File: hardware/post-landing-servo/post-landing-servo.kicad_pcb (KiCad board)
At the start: 2 copper layers, 0 parts

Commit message: Gavin and Remco pcb to be checked
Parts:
- added G***: LOGO, LOGO, F.Cu at (42.9, 54.5)
- added G***: LOGO, LOGO, F.Cu at (100.3, 58.1)
- added G***: LOGO, LOGO, F.Cu at (98.7, 38.8)
- added G***: LOGO, LOGO, F.Cu at (100.0, 47.8)
- added H1: MountingHole_Pad, MountingHole:MountingHole_3.2mm_M3_Pad_Via, F.Cu at (57.2, 36.1)
- added H2: MountingHole_Pad, MountingHole:MountingHole_3.2mm_M3_Pad_Via, F.Cu at (83.2, 59.1)
- added J1: Conn_01x08, Custom:ZH-6PWB_knockoff, F.Cu at (60.0, 58.2)
- added J2: DE9_Pins, Connector_Dsub:DSUB-9_Pins_Horizontal_P2.77x2.84mm_EdgePinOffset4.94mm_Housed_MountingHolesOffset4.94mm, F.Cu at (50.6, 41.8)
- added J3: DE9_Pins, Connector_Dsub:DSUB-9_Pins_Horizontal_P2.77x2.84mm_EdgePinOffset4.94mm_Housed_MountingHolesOffset4.94mm, F.Cu at (89.5, 52.8)
- added J4: Conn_01x08, Custom:ZH-6PWB_knockoff, F.Cu at (73.2, 58.3)
- added J5: Conn_01x06, Connector_JST:JST_EH_B6B-EH-A_1x06_P2.50mm_Vertical, F.Cu at (64.8, 34.6)
- added JP1: SolderJumper_2_Open, Jumper:SolderJumper-2_P1.3mm_Bridged_Pad1.0x1.5mm, F.Cu at (63.5, 41.8)
- added JP2: SolderJumper_2_Open, Jumper:SolderJumper-2_P1.3mm_Bridged_Pad1.0x1.5mm, F.Cu at (63.6, 45.6)
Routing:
- net +5V: track 0.00 -> 126.1 mm
- net /CAN_A+: track 0.00 -> 109.2 mm
- net /CAN_A-: track 0.00 -> 108.7 mm
- net +24V: track 0.00 -> 98.6 mm
- net /SIG2: track 0.00 -> 72.3 mm, vias 0 -> 1
- net /SIG1: track 0.00 -> 68.7 mm, vias 0 -> 1
- net /CAN_B+: track 0.00 -> 64.8 mm
- net /CAN_B-: track 0.00 -> 64.7 mm
- net GND: track 0.00 -> 40.2 mm
- added copper zone on B.Cu, net GND
- added copper zone on F.Cu, net GND
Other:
- board outline added: 70.3 x 32.8 mm
- board text added: "67 67 67 67 67 67 67 67 67 67 67"
- board text added: "Designed by: Gavin, H. & Remco, S."

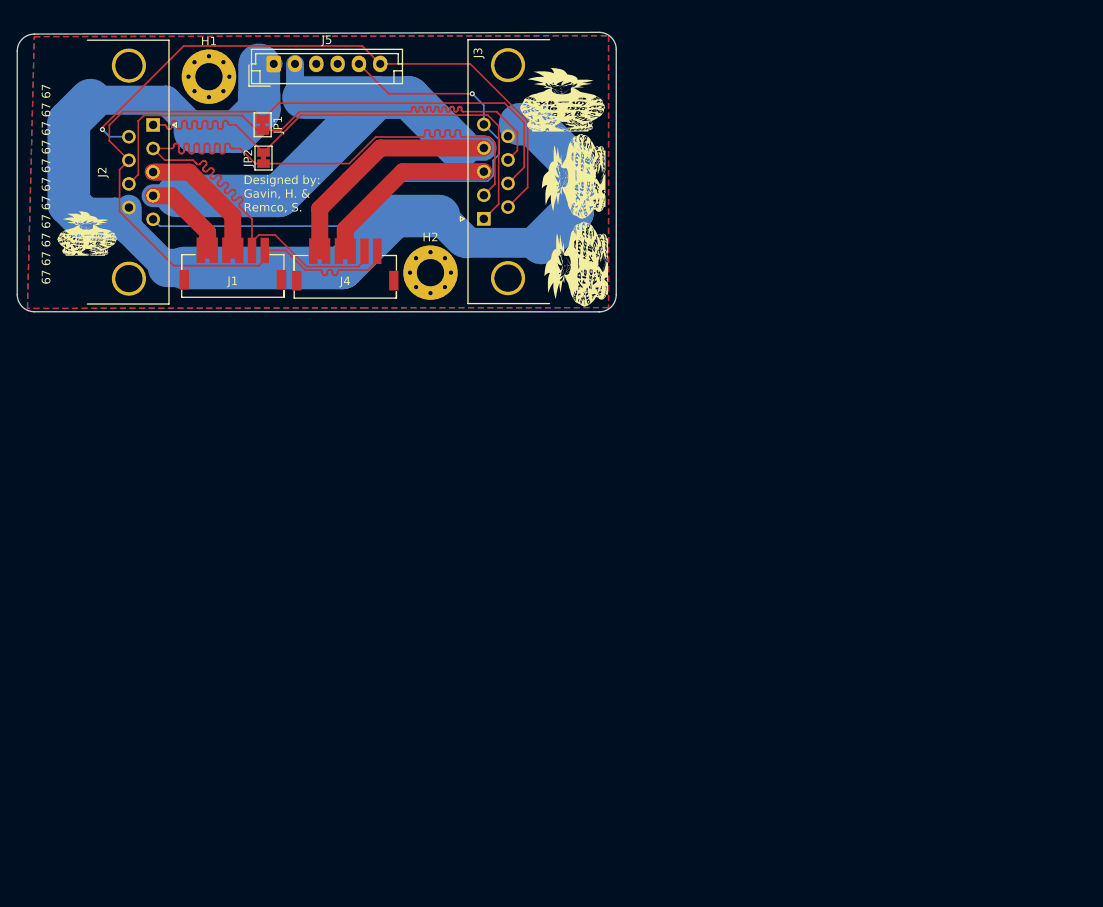
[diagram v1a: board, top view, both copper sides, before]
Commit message: fix: Changed DE-9 headers to female
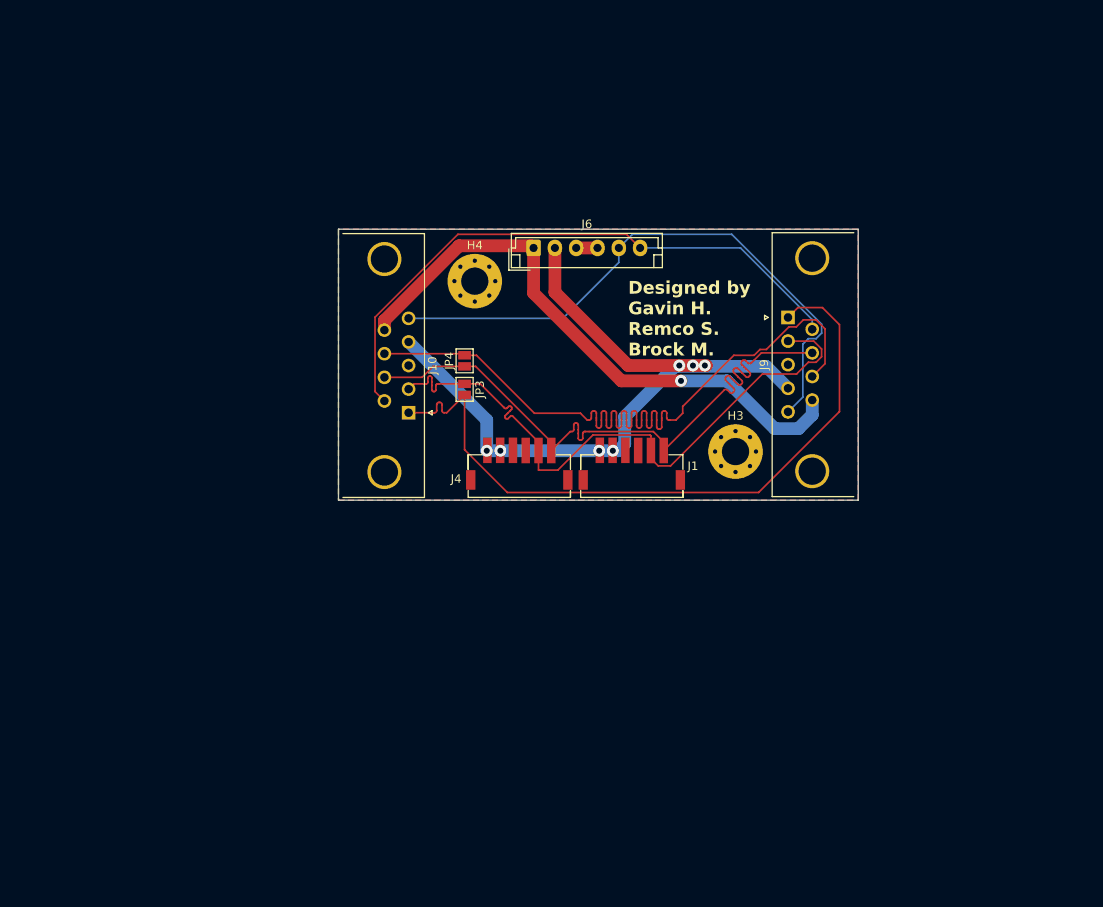
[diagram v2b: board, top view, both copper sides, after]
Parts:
- removed G*** (x4): LOGO, LOGO
- removed H1, H2: MountingHole_Pad, MountingHole:MountingHole_3.2mm_M3_Pad_Via
- removed J2, J3: DE9_Pins, Connector_Dsub:DSUB-9_Pins_Horizontal_P2.77x2.84mm_EdgePinOffset4.94mm_Housed_MountingHolesOffset4.94mm
- removed J5: Conn_01x06, Connector_JST:JST_EH_B6B-EH-A_1x06_P2.50mm_Vertical
- removed JP1, JP2: SolderJumper_2_Open, Jumper:SolderJumper-2_P1.3mm_Bridged_Pad1.0x1.5mm
- added H3: MountingHole_Pad, MountingHole:MountingHole_3.2mm_M3_Pad_Via, F.Cu at (119.0, 80.1)
- added H4: MountingHole_Pad, MountingHole:MountingHole_3.2mm_M3_Pad_Via, F.Cu at (88.4, 60.1)
- added J10: DE9_Socket, Connector_Dsub:DSUB-9_Socket_Horizontal_P2.77x2.84mm_EdgePinOffset4.94mm_Housed_MountingHolesOffset4.94mm, F.Cu at (80.6, 75.5)
- added J6: Conn_01x06, Connector_JST:JST_EH_B6B-EH-A_1x06_P2.50mm_Vertical, F.Cu at (95.3, 56.2)
- added J9: DE9_Socket, Connector_Dsub:DSUB-9_Socket_Horizontal_P2.77x2.84mm_EdgePinOffset4.94mm_Housed_MountingHolesOffset4.94mm, F.Cu at (125.2, 64.4)
- added JP3: SolderJumper_2_Open, Jumper:SolderJumper-2_P1.3mm_Open_Pad1.0x1.5mm, F.Cu at (87.2, 72.8)
- added JP4: SolderJumper_2_Open, Jumper:SolderJumper-2_P1.3mm_Open_Pad1.0x1.5mm, F.Cu at (87.2, 69.5)
- moved J1 52.4 mm to (106.8, 81.7)
- moved J4 31.1 mm to (93.6, 81.7)
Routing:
- net +5V: track 126.1 -> 69.4 mm, vias 0 -> 1
- net GND: track 40.2 -> 2.50 mm
- net /CAN_A+: track 109.2 -> 75.4 mm
- net /CAN_A-: track 108.7 -> 75.5 mm
- net /CAN_B+: track 64.8 -> 93.4 mm
- net /CAN_B-: track 64.7 -> 83.4 mm
- net +24V: track 98.6 -> 85.5 mm, vias 0 -> 7
- net /SIG1: track 68.7 -> 70.4 mm, vias 1 -> 0
- net /SIG2: track 72.3 -> 70.9 mm, vias 1 -> 0
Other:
- board size 70.3 x 32.8 mm -> 61 x 31.8 mm
- board text added: "Designed by Gavin H. Remco S. Brock M."
- board text removed: "67 67 67 67 67 67 67 67 67 67 67"
- board text removed: "Designed by: Gavin, H. & Remco, S."

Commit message: Feat: Reroute and minor fixes
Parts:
- removed J1, J4: Conn_01x08, Custom:ZH-6PWB_knockoff
- removed J6: Conn_01x06, Connector_JST:JST_EH_B6B-EH-A_1x06_P2.50mm_Vertical
- added 5V    24V   GND    PWM1 PWM2: Conn_01x06, Connector_JST:JST_EH_B6B-EH-A_1x06_P2.50mm_Vertical, F.Cu at (123.8, 102.3)
- added RMD-A: Conn_01x06, Connector_JST:JST_ZH_B6B-ZR-SM4-TF_1x06-1MP_P1.50mm_Vertical, F.Cu at (121.0, 127.8)
- added RMD-B: Conn_01x06, Connector_JST:JST_ZH_B6B-ZR-SM4-TF_1x06-1MP_P1.50mm_Vertical, F.Cu at (139.0, 127.8)
- moved JP4 77.3 mm to (146.3, 119.3), turned to -90 degrees
- moved JP3 72.9 mm to (146.3, 115.4), turned to 90 degrees
- moved H4 72.2 mm to (145.0, 105.0)
- moved J9 53.1 mm to (152.3, 110.0)
- moved J10 52.9 mm to (107.7, 121.0)
- moved H3 40.1 mm to (115.0, 120.0)
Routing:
- net /CAN_B+: track 93.4 -> 54.4 mm, vias 0 -> 1
- net /CAN_B-: track 83.4 -> 49.8 mm, vias 0 -> 1
- net +24V: track 85.5 -> 107.9 mm, vias 7 -> 6
- net /SIG1: track 70.4 -> 56.8 mm, vias 0 -> 1
- net /CAN_A+: track 75.4 -> 85.4 mm, vias 0 -> 4
- net GND: track 2.50 -> 0.00 mm, vias 0 -> 10
- net /SIG2: track 70.9 -> 73.4 mm
- net /CAN_A-: track 75.5 -> 77.9 mm, vias 0 -> 4
- net +5V: track 69.4 -> 68.8 mm, vias 1 -> 0
- added copper zone on F.Cu, net +24V
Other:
- board size 61 x 31.8 mm -> 60 x 32 mm
- board text added: "24V"
- board text added: "5V"
- board text added: "GND"
- board text added: "I should be in a case! Please?"
- board text added: "Jump to terminate here"
- board text added: "PWM0"
- board text added: "PWM1"
- board text added: "Servo CAN propagation board"
- board text removed: "Designed by Gavin H. Remco S. Brock M."
